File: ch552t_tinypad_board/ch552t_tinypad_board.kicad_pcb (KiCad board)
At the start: 2 copper layers, 91 x 55 mm, 26 parts, among them J1 Conn_02x10_Odd_Even, J2 USB_C_Receptacle_USB2.0, SW1 SW_Push, SW2 SW_Push, SW3 SW_Push, SW4 SW_Push, SW5 SW_Push, SW6 SW_Push, SW7 SW_Push, U1 CH552T

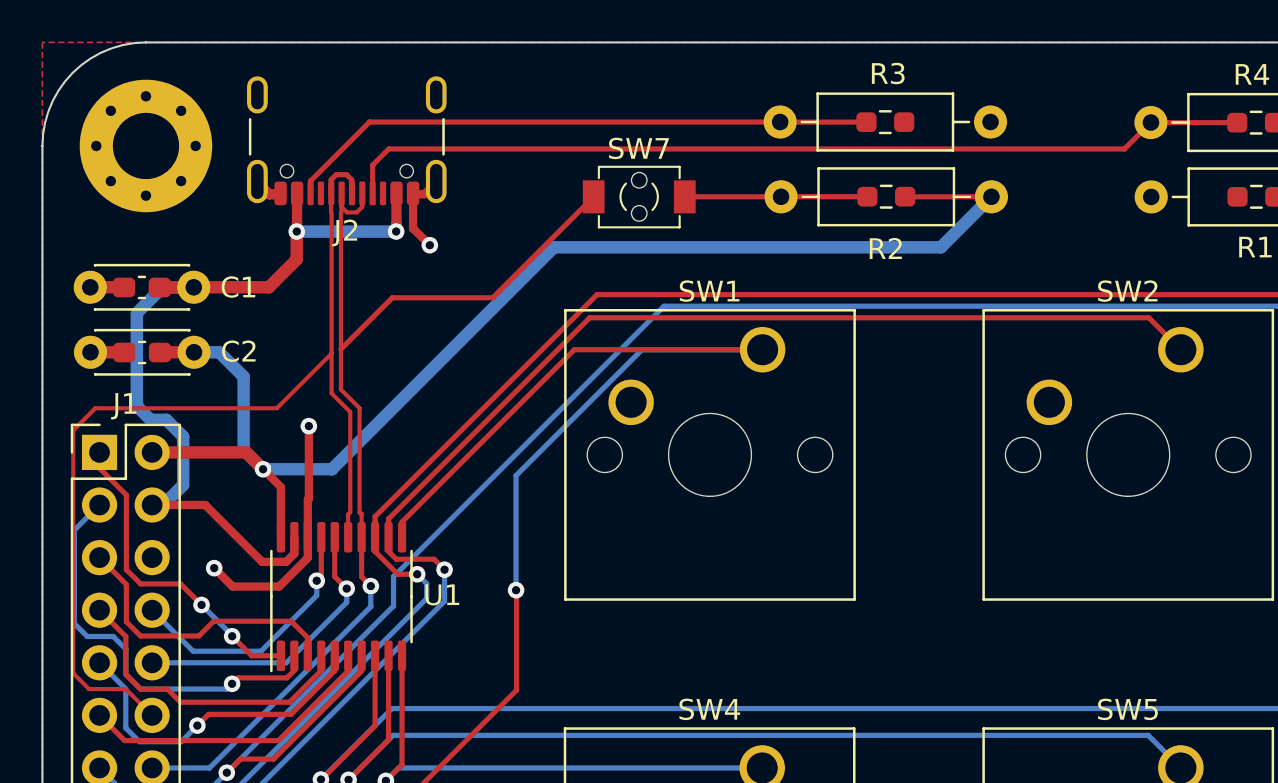
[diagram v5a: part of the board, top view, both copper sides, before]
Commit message: feat: straighten diff pair of USB
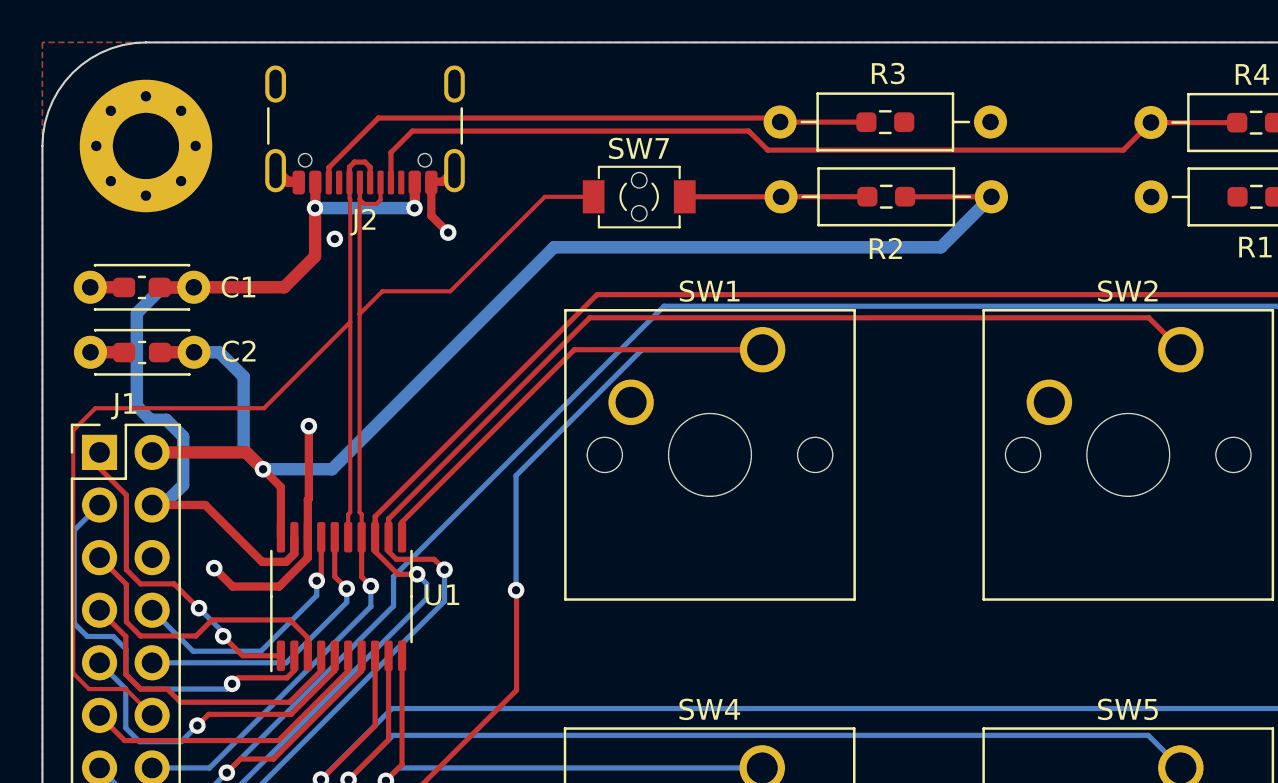
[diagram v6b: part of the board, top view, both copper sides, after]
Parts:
- moved J2 1.02 mm to (54.6, 34.1)
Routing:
- net VCC: track 40.0 -> 41.9 mm
- net /D-: track 50.0 -> 51.8 mm
- net Net-(J2-CC2): track 28.7 -> 27.7 mm
- net GND: vias 3 -> 4

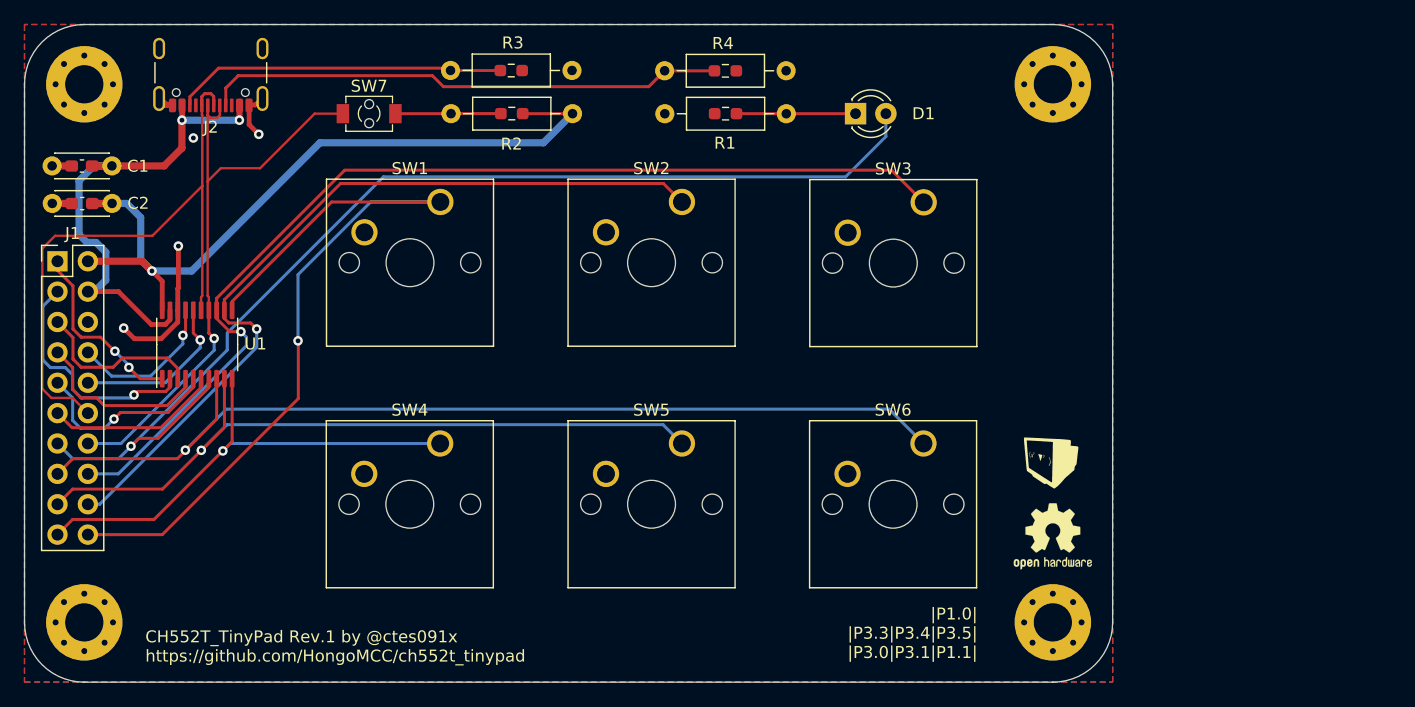
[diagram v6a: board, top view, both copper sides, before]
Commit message: hotfix: replace swapped USB differential pair
pcb is not fixed
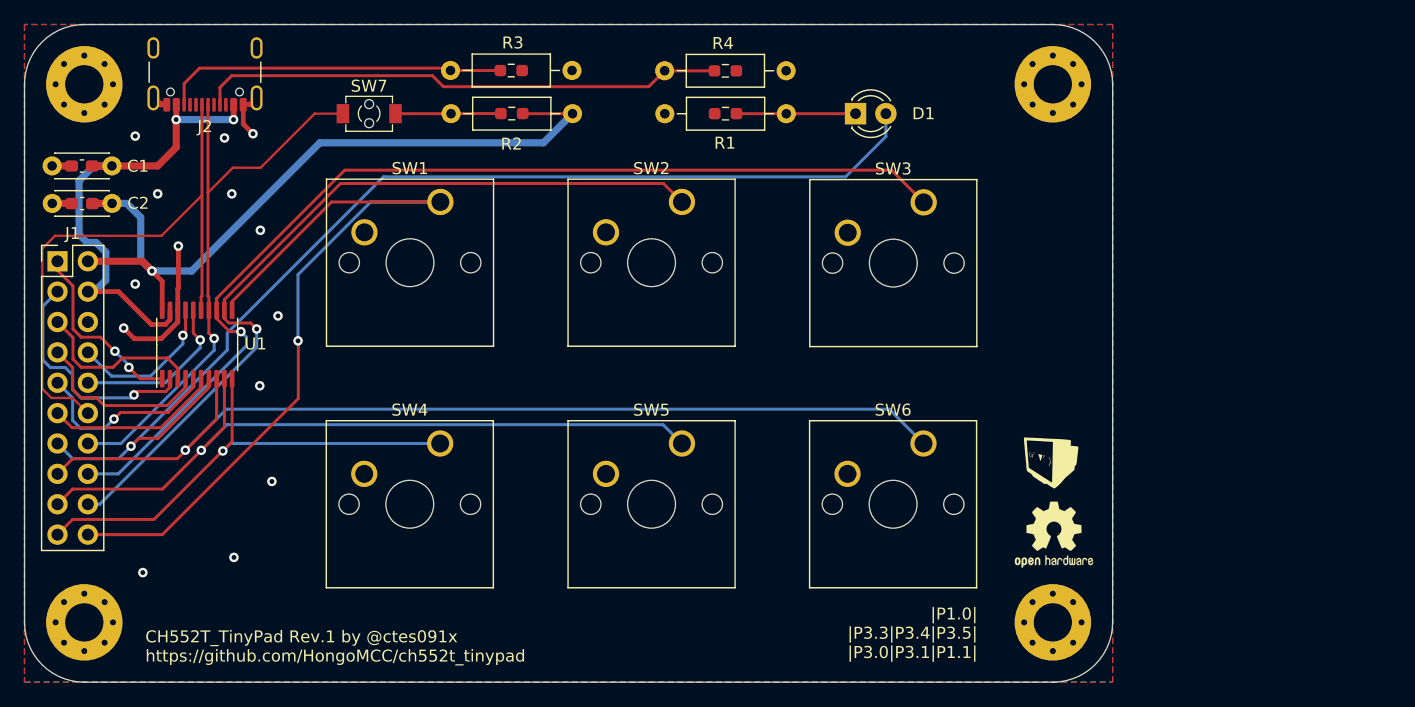
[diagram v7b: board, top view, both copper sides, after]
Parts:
- moved J2 0.49 mm to (54.1, 34.0)
- moved REF** 0.17 mm to (125.1, 73.7)
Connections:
- J2 pad A6: /D- -> /D+
- J2 pad A7: /D+ -> /D-
- J2 pad B6: /D- -> /D+
- J2 pad B7: /D+ -> /D-
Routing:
- net /D+: track 51.9 -> 48.8 mm
- net /D-: track 51.8 -> 48.8 mm
- net Net-(J2-CC2): track 27.7 -> 28.8 mm
- net GND: vias 4 -> 14

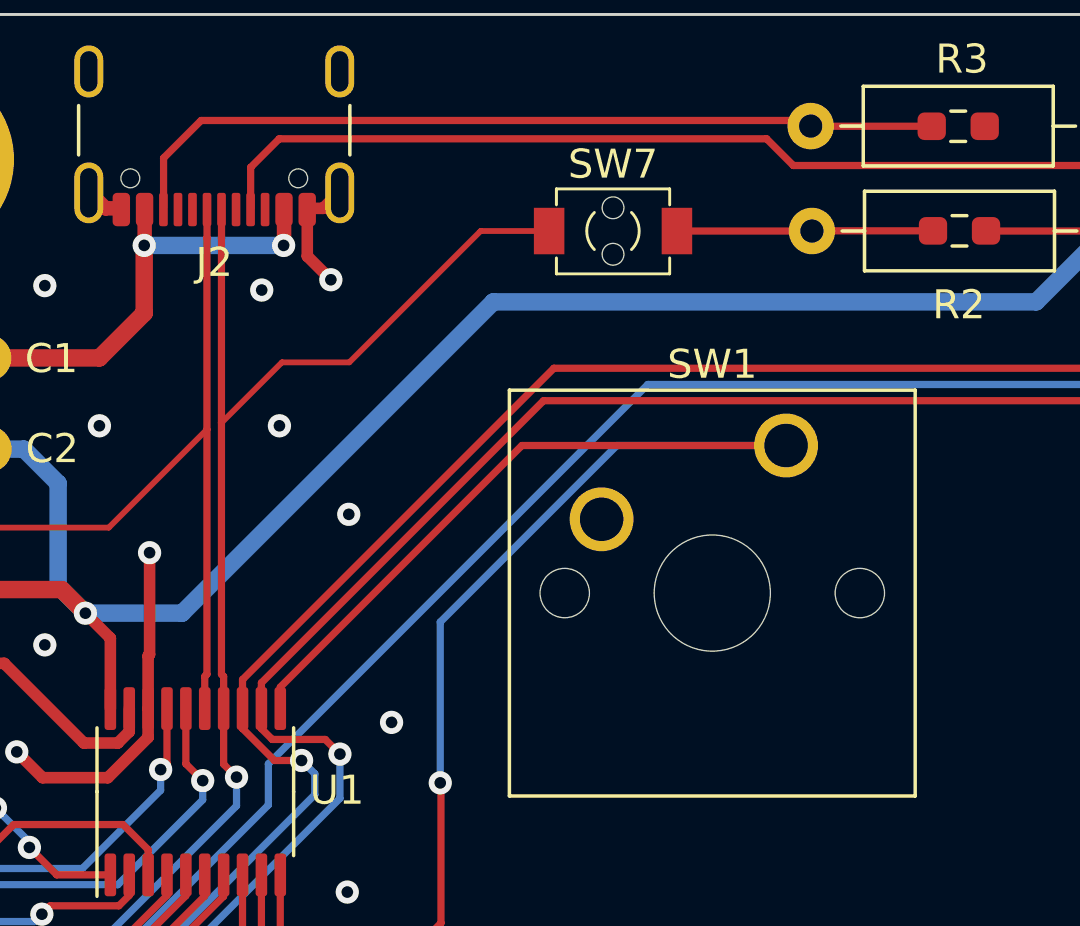
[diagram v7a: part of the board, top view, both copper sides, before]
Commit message: fix: rewire USB diff pair
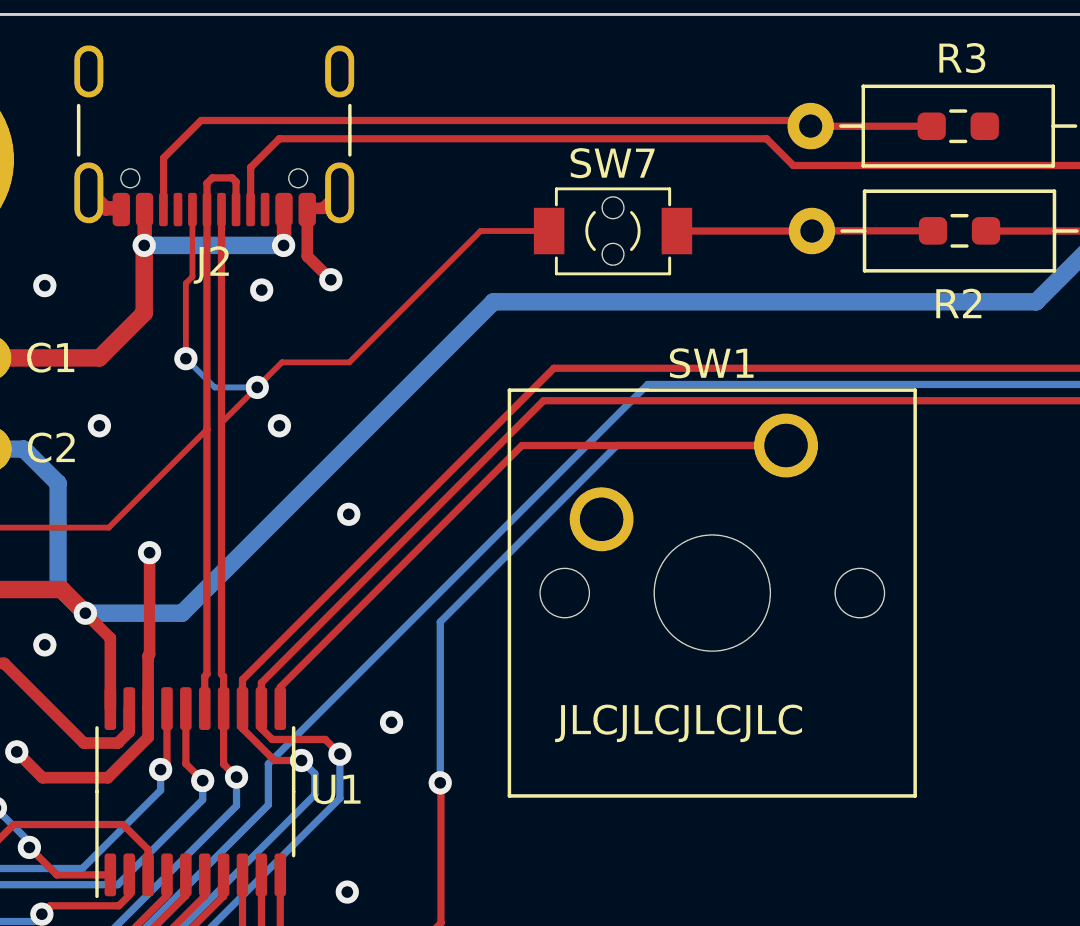
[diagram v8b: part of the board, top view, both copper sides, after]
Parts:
- C1, C2: value C -> 0.1u
- R1, R2: value R -> 10k
- R3, R4: value R -> 5.1k
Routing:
- net /D+: track 48.8 -> 56.9 mm, vias 1 -> 3
- net /D-: track 48.8 -> 51.8 mm
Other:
- board text added: "JLCJLCJLCJLC"
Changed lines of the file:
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@@
       (outputformat 1)
       (mirror false)
-      (drillshape 1)
+      (drillshape 0)
       (scaleselection 1)
-      (outputdirectory "")
+      (outputdirectory "gerber/")
     )
   )
@@
       (net 2 "GND") (pinfunction "1") (pintype "input"))
   )
-  (footprint "Symbol:OSHW-Logo2_7.3x6mm_SilkScreen" (layer "F.Cu")
+  (footprint "Symbol:OSHW-Logo2_7.3x6mm_SilkScreen" locked (layer "F.Cu")
     (at 125.095 73.66)
     (descr "Open Source Hardware Symbol")
@@
         (effects (font (size 1 1) (thickness 0.15)))
     )
-    (fp_text value "R" (at 5.08 2.3876 180 unlocked) (layer "F.Fab")
+    (fp_text value "10k" (at -2.701124 0.0061 unlocked) (layer "F.Fab")
         (effects (font (size 1 1) (thickness 0.15)))
     )
-    (fp_text user "${REFERENCE}" (at 5.08 3.6576 180 unlocked) (layer "F.Fab")
+    (fp_text user "${REFERENCE}" (at 5.058876 -0.0383 unlocked) (layer "F.Fab")
         (effects (font (size 1 1) (thickness 0.15)))
     )
@@
         (effects (font (size 1 1) (thickness 0.15)))
     )
-    (fp_text user "${REFERENCE}" (at 0 0 90) (layer "F.Fab")
+    (fp_text user "${REFERENCE}" (at 0 0 180) (layer "F.Fab")
         (effects (font (size 1 1) (thickness 0.15)))
     )
@@
         (effects (font (size 1 1) (thickness 0.15)))
     )
-    (fp_text value "R" (at 5.08 2.3876 unlocked) (layer "F.Fab")
+    (fp_text value "5.1k" (at 13.281576 0.0061 unlocked) (layer "F.Fab")
         (effects (font (size 1 1) (thickness 0.15)))
     )
@@
         (effects (font (size 1 1) (thickness 0.15)))
     )
-    (fp_text value "R" (at 5.08 2.3876 180 unlocked) (layer "F.Fab")
+    (fp_text value "10k" (at -2.824324 -0.0508 unlocked) (layer "F.Fab")
         (effects (font (size 1 1) (thickness 0.15)))
     )
@@
         (effects (font (size 1 1) (thickness 0.15)))
     )
-    (fp_text value "USB_C_Receptacle_USB2.0" (at 0 5 180 unlocked) (layer "F.Fab")
+    (fp_text value "USB_C_Receptacle_USB2.0" (at 0 5 unlocked) (layer "F.Fab")
         (effects (font (size 1 1) (thickness 0.15)))
     )
@@
         (effects (font (size 1 1) (thickness 0.15)))
     )
-    (fp_text value "C" (at 2.504847 2.12 180 unlocked) (layer "F.Fab")
+    (fp_text value "0.1u" (at 5.559053 -0.0256 unlocked) (layer "F.Fab")
         (effects (font (size 1 1) (thickness 0.15)))
     )
-    (fp_text user "${REFERENCE}" (at 2.504847 3.62 180 unlocked) (layer "F.Fab")
+    (fp_text user "${REFERENCE}" (at 0.009053 -0.0256 unlocked) (layer "F.Fab")
         (effects (font (size 1 1) (thickness 0.15)))
     )
@@
         (effects (font (size 1 1) (thickness 0.15)))
     )
-    (fp_text value "R" (at 5.08 2.3876 unlocked) (layer "F.Fab")
+    (fp_text value "5.1k" (at 13.165176 0.0319 unlocked) (layer "F.Fab")
         (effects (font (size 1 1) (thickness 0.15)))
     )
-    (fp_text user "${REFERENCE}" (at 5.08 3.6576 unlocked) (layer "F.Fab")
+    (fp_text user "${REFERENCE}" (at 5.065176 0.0319 unlocked) (layer "F.Fab")
         (effects (font (size 1 1) (thickness 0.15)))
     )
@@
         (effects (font (size 1 1) (thickness 0.15)))
     )
-    (fp_text value "C" (at 2.504847 2.12 180 unlocked) (layer "F.Fab")
+    (fp_text value "0.1u" (at 5.520947 0.014 unlocked) (layer "F.Fab")
         (effects (font (size 1 1) (thickness 0.15)))
     )
-    (fp_text user "${REFERENCE}" (at 2.504847 3.62 180 unlocked) (layer "F.Fab")
+    (fp_text user "${REFERENCE}" (at 0.004847 -0.036 unlocked) (layer "F.Fab")
         (effects (font (size 1 1) (thickness 0.15)))
     )
@@
     (effects (font (size 1 1) (thickness 0.15)) (justify left bottom))
   )
+  (gr_text "JLCJLCJLCJLC" (at 65.9 55.9) (layer "F.SilkS")
+    (effects (font (size 1 1) (thickness 0.15)) (justify left bottom))
+  )
   (dimension (type aligned) (layer "Eco1.User")
     (pts (xy 39 31) (xy 44 31))
@@
   (segment (start 53.6956 57.3786) (end 53.6956 58.039) (width 0.25) (layer "B.Cu") (net 11))
   (segment (start 50.7746 60.96) (end 44.2976 60.96) (width 0.25) (layer "B.Cu") (net 11))
+  (segment (start 53.844 36.8086) (end 54.0258 36.6268) (width 0.25) (layer "F.Cu") (net 12))
+  (segment (start 54.0258 36.6268) (end 54.7116 36.6268) (width 0.25) (layer "F.Cu") (net 12))
+  (segment (start 54.844 36.7592) (end 54.844 37.716) (width 0.25) (layer "F.Cu") (net 12))
   (segment (start 41.2496 62.23) (end 40.4876 61.468) (width 0.2) (layer "F.Cu") (net 12))
   (segment (start 53.844 38.698029) (end 53.844 37.716) (width 0.25) (layer "F.Cu") (net 12))
+  (segment (start 54.7116 36.6268) (end 54.844 36.7592) (width 0.25) (layer "F.Cu") (net 12))
   (segment (start 53.8416 38.700429) (end 53.844 38.698029) (width 0.25) (layer "F.Cu") (net 12))
   (segment (start 44.2976 63.5) (end 43.0276 62.23) (width 0.2) (layer "F.Cu") (net 12))
@@
   (segment (start 53.8416 53.715849) (end 53.8416 45.2882) (width 0.25) (layer "F.Cu") (net 12))
   (segment (start 41.5544 48.6664) (end 50.4634 48.6664) (width 0.2) (layer "F.Cu") (net 12))
+  (segment (start 53.844 37.716) (end 53.844 36.8086) (width 0.25) (layer "F.Cu") (net 12))
   (segment (start 54.4166 56.812798) (end 54.4166 54.8971) (width 0.25) (layer "F.Cu") (net 13))
+  (segment (start 55.5752 43.826) (end 55.5752 43.8404) (width 0.2) (layer "F.Cu") (net 13))
   (segment (start 65.613076 38.4556) (end 65.435276 38.6334) (width 0.25) (layer "F.Cu") (net 13))
   (segment (start 54.344 38.698029) (end 54.344 37.716) (width 0.25) (layer "F.Cu") (net 13))
+  (segment (start 53.1171 42.8498) (end 53.1171 40.2533) (width 0.2) (layer "F.Cu") (net 13))
+  (segment (start 55.5608 43.8404) (end 54.3416 45.0596) (width 0.2) (layer "F.Cu") (net 13))
   (segment (start 58.7432 42.9768) (end 56.4244 42.9768) (width 0.2) (layer "F.Cu") (net 13))
+  (segment (start 55.5752 43.8404) (end 55.5608 43.8404) (width 0.2) (layer "F.Cu") (net 13))
   (segment (start 54.860627 57.256825) (end 54.4166 56.812798) (width 0.25) (layer "F.Cu") (net 13))
   (segment (start 63.2644 38.4556) (end 58.7432 42.9768) (width 0.2) (layer "F.Cu") (net 13))
   (segment (start 54.3416 38.700429) (end 54.344 38.698029) (width 0.25) (layer "F.Cu") (net 13))
   (segment (start 54.3416 53.715849) (end 54.3416 45.0596) (width 0.25) (layer "F.Cu") (net 13))
+  (segment (start 53.344 40.0264) (end 53.344 37.716) (width 0.2) (layer "F.Cu") (net 13))
   (segment (start 54.4166 54.8971) (end 54.4166 53.790849) (width 0.25) (layer "F.Cu") (net 13))
   (segment (start 54.3416 45.0596) (end 54.3416 38.700429) (width 0.25) (layer "F.Cu") (net 13))
-  (segment (start 56.4244 42.9768) (end 54.3416 45.0596) (width 0.2) (layer "F.Cu") (net 13))
+  (segment (start 53.1171 40.2533) (end 53.344 40.0264) (width 0.2) (layer "F.Cu") (net 13))
+  (segment (start 56.4244 42.9768) (end 55.5752 43.826) (width 0.2) (layer "F.Cu") (net 13))
   (segment (start 54.4166 53.790849) (end 54.3416 53.715849) (width 0.25) (layer "F.Cu") (net 13))
   (segment (start 65.622876 38.4556) (end 63.2644 38.4556) (width 0.2) (layer "F.Cu") (net 13))
   (via (at 54.860627 57.256825) (size 0.8) (drill 0.4) (layers "F.Cu" "B.Cu") (net 13))
+  (via (at 53.1171 42.8498) (size 0.8) (drill 0.4) (layers "F.Cu" "B.Cu") (net 13))
+  (via (at 55.5752 43.8404) (size 0.8) (drill 0.4) (layers "F.Cu" "B.Cu") (net 13))
+  (segment (start 53.1171 42.8498) (end 54.1077 43.8404) (width 0.2) (layer "B.Cu") (net 13))
   (segment (start 47.0662 66.04) (end 44.2976 66.04) (width 0.25) (layer "B.Cu") (net 13))
   (segment (start 54.860627 58.245573) (end 47.0662 66.04) (width 0.25) (layer "B.Cu") (net 13))
   (segment (start 54.860627 57.256825) (end 54.860627 58.245573) (width 0.25) (layer "B.Cu") (net 13))
+  (segment (start 54.1077 43.8404) (end 55.5752 43.8404) (width 0.2) (layer "B.Cu") (net 13))
   (segment (start 111.506 43.18) (end 65.786 43.18) (width 0.25) (layer "F.Cu") (net 14))
   (segment (start 114.1984 45.8724) (end 111.506 43.18) (width 0.25) (layer "F.Cu") (net 14))
